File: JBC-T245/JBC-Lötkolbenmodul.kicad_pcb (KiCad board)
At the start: 2 copper layers, 159 x 50 mm, 99 parts, among them IC101 ATMEGA328P-A, IC102 SP3485EN, IC103 INA193, IC104 CNY17-1, K101 XLR5, K102 Lötkolben_1_CONN_3, P101 CONN_01X03, P102 CONN_3X2, P103 2 externe Pins, P104 CONN_01X01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

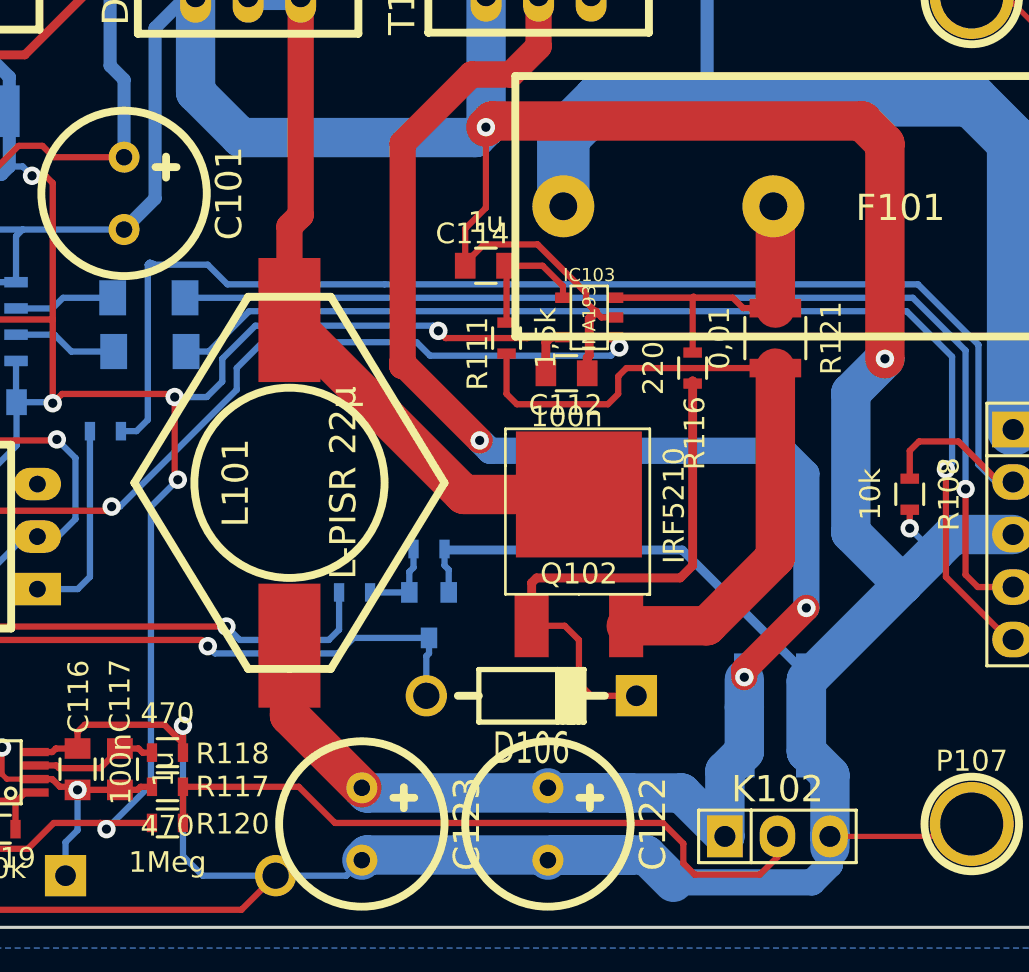
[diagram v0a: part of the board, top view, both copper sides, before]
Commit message: schutz für den Temperaturmesswandler verbessert
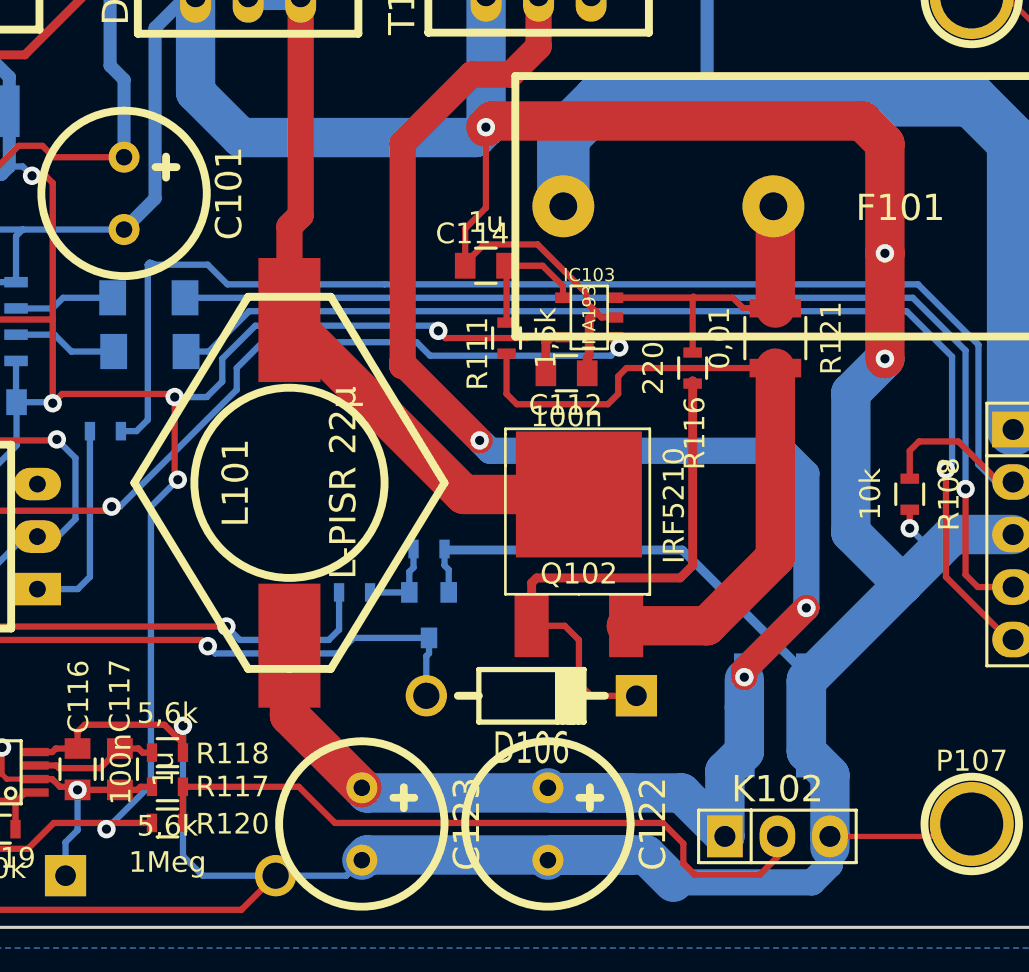
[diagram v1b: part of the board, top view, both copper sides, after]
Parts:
- R117, R118: value 470 -> 5,6k
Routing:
- net GND: vias 16 -> 17
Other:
- rule trace_min: 0.254 -> 0.2032

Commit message: Programm angefangen.
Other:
- board text added: "die duo-LED wird durch eine WS2812B ersetzt, da sie so vielseitiger anzeigen kann."

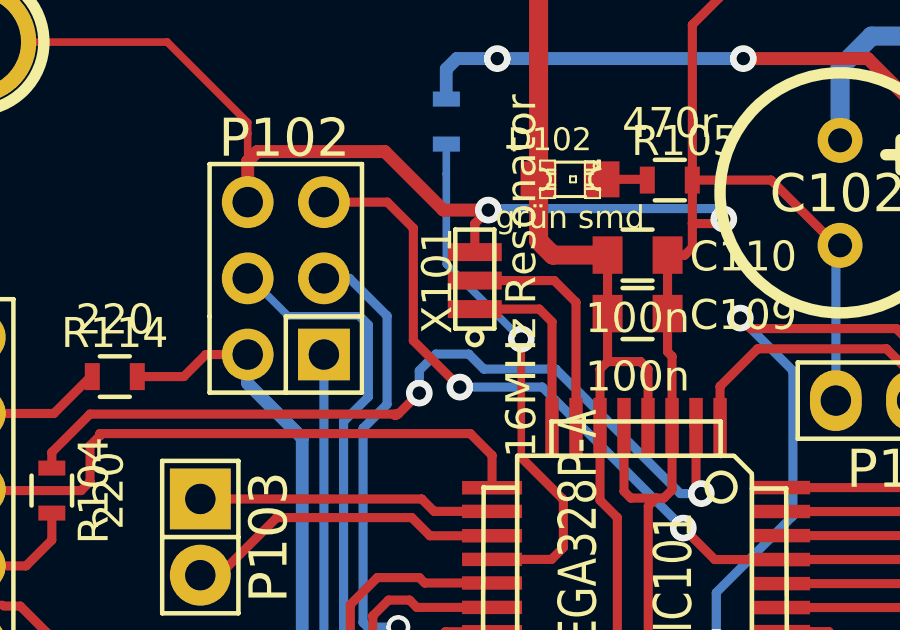
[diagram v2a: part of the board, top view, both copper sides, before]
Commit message: fehlerhaftes footprint des 16MHz resonators. fixed. programm geht los.
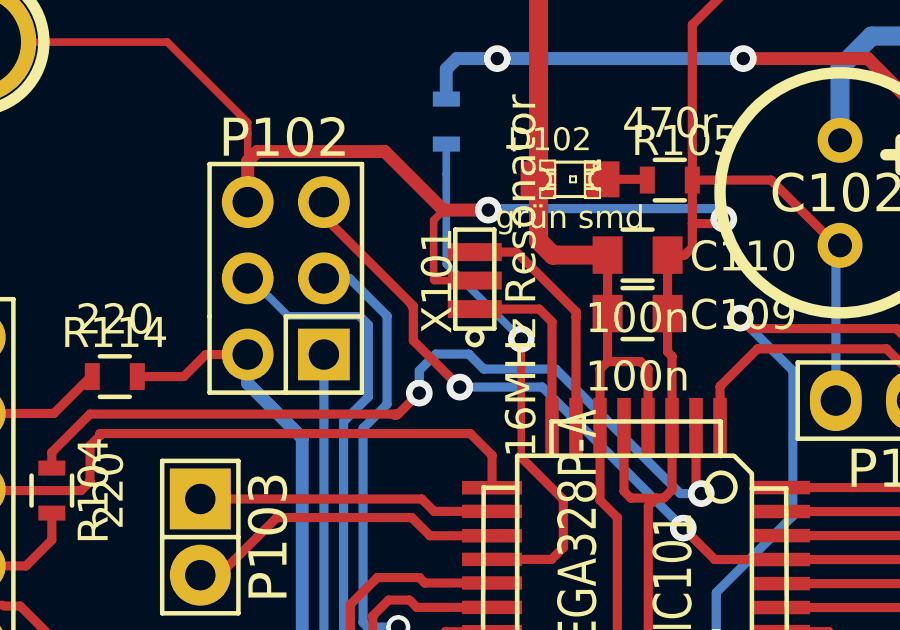
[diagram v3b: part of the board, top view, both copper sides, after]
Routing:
- net GND: track 741.3 -> 743.6 mm
- net /reset: track 48.9 -> 47.7 mm
